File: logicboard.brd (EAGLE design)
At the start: 160 x 100 mm, 17 parts, among them U1 RASPBERRY_PI_CM-1-1376408-4, X3 PCI-60-POS-145167, X4 PCI-60-POS-145167, X5 PCI-60-POS-145167

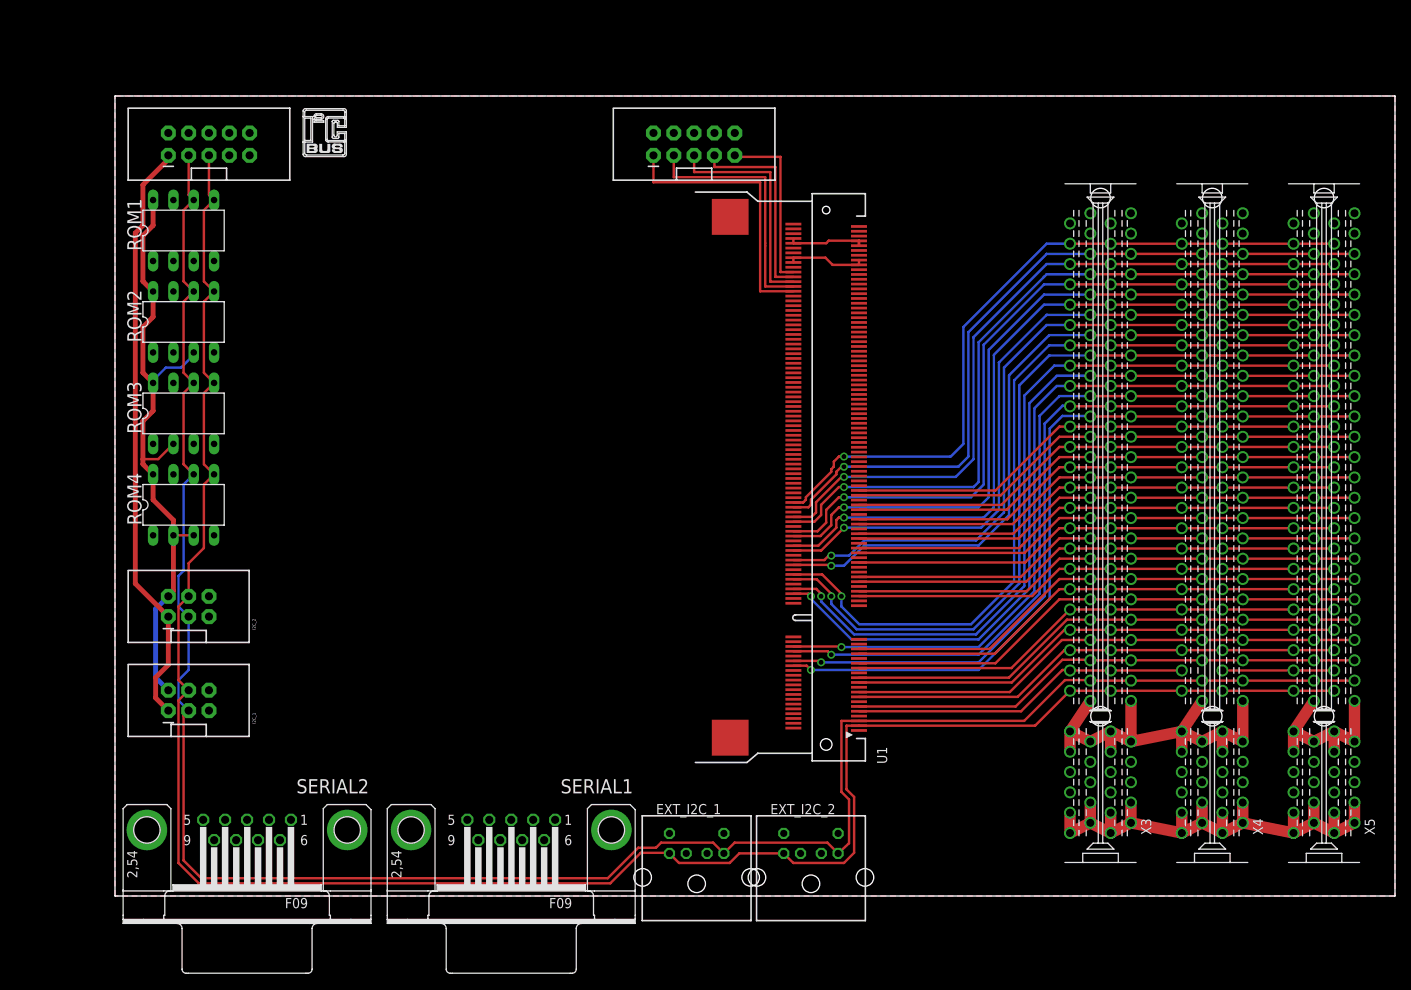
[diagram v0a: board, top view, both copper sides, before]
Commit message: Initial board, probably scrap
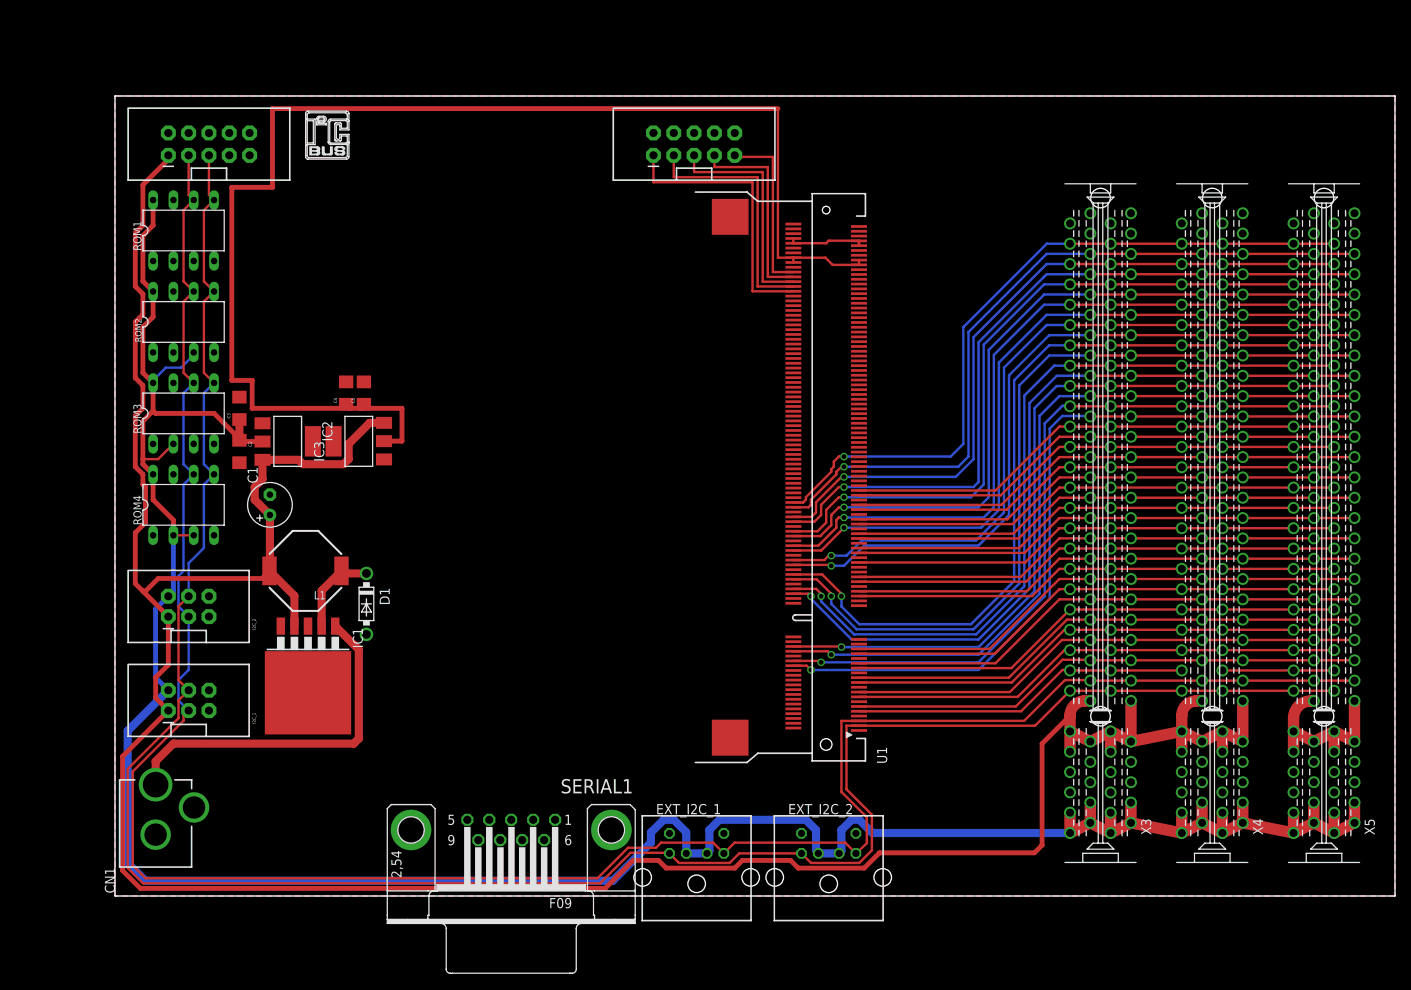
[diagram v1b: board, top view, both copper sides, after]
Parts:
- removed SERIAL2: (no value), con-subd:F09HP
- added C1: 220uf, rcl:E2,5-6
- added C2, C3, C4, C5: (no value), SparkFun-Capacitors:1206
- added CN1: (no value), adafruit:DCJACK_2MM_PTH
- added D1: 1N5824, diode:DO41-7.6
- added IC1: (no value), linear:TO263-5
- added IC2, IC3: REG1117, burr-brown:SOT223
- added L1: (no value), SparkFun-Passives:SRU1038
- moved EXT_I2C_2 2.22 mm to (89.2, -3.17)
- moved U$1 0.45 mm to (23.8, 92.1)
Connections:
- new net GNDBREAK: CN1.GNDBREAK
- new net V+: CN1.PWR, IC1.1
- new net VOUT: D1.C, IC1.2, L1.1
- net 1.8V: now also C4.1, C5.1, IC3.2
- net 3.3V: now also C2.1, C3.1, IC2.2
- net 5V: now also C1.+, IC1.4, IC2.3, IC3.3, L1.2
- net GND: now also C1.-, C2.2, C3.2, C4.2, C5.2, CN1.GND, D1.A, IC1.3, IC1.5, IC1.6, IC2.1, IC3.1
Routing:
- net 5V: track 150.4 -> 373.4 mm
- net 3.3V: track 160.4 -> 338.8 mm
- net 1.8V: track 9.77 -> 165.0 mm
- net V+: track 0.00 -> 44.8 mm
- net SCL: track 264.3 -> 276.8 mm
- net SDA: track 263.0 -> 275.3 mm
- net VOUT: track 0.00 -> 11.2 mm

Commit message: Initial commit
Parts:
- removed JP1: (no value), SparkFun-Connectors:2X5-SHROUDED_LOCK
- removed X3, X4, X5: PCI-60-POS-145167, con-amp:145167-2
- added AUDIO: (no value), SparkFun-Connectors:AUDIO-JACK
- added C10, C13: 0.01uf, SparkFun-Capacitors:CAP-PTH-SMALLEZ
- added C11, C14: 100uf, SparkFun-Capacitors:CAP-PTH-SMALLEZ
- added C12, C15: 0.001uf, SparkFun-Capacitors:CAP-PTH-SMALLEZ
- added C16, C17: (no value), SparkFun-Capacitors:1206
- added C6, C7: 10uf, SparkFun-Capacitors:CAP-PTH-SMALLEZ
- added C8, C9: 33n, SparkFun-Capacitors:CAP-PTH-SMALLEZ
- added CHEATER: (no value), SparkFun-Connectors:2X8
- added EXP1, EXP2, EXP3, EXP4, EXP5, EXP6, VIDEOCORE_JTAG: (no value), SparkFun-Connectors:2X5-SHROUDED_LOCK
- added H1, H2, H3, H4, H5, H6, H7, H8: MOUNT-HOLE4.5, holes:4,5
- added IC4: MCP2300X/P, adafruit:DIL18
- added IC5: REG1117, burr-brown:SOT223
- added PWR_SWITCH: (no value), SparkFun-Connectors:MOLEX-1X2
- added Q2: MOSFET-NCHANNELBS170, SparkFun-DiscreteSemi:TO-92
- added R1, R2: 10k, SparkFun-Resistors:AXIAL-0.3EZ
- added R3, R4: 150r, SparkFun-Resistors:AXIAL-0.3EZ
- added R5, R6: 270R, SparkFun-Resistors:AXIAL-0.3EZ
- added R7: (no value), SparkFun-Resistors:RPACK-SIP-PTH-8
- added R8, R9: (no value), SparkFun-Resistors:AXIAL-0.3EZ
- added SERIAL1_PORTFLIP, USB_POLARITY: FEMALE 2x3, SparkFun-Connectors:2X3
- added SPKR_L, SPKR_R: (no value), SparkFun-Connectors:JST-2-PTH-KIT
- added U$2: TDA7052, tda7052:DIL08
- U$1: value (none) -> TDA7052; device micro-philips:I2C -> tda7052:DIL08
- moved FRONTPANEL 131.6 mm to (137.8, 56.2), turned to 0 degrees
- moved L1 127.4 mm to (151.1, 37.5)
- moved IC1 127.3 mm to (151.4, 25.1)
- moved D1 126.7 mm to (158.1, 33.7)
- moved C1 123.7 mm to (142.6, 37.5), turned to 180 degrees
- moved C3 122.2 mm to (134.6, 33.7), turned to 0 degrees
- moved C2 121.5 mm to (134.6, 31.4), turned to 0 degrees
- moved U$1 120.4 mm to (144.1, 88.6), turned to 270 degrees
- moved IC2 116.2 mm to (133.3, 25.1), turned to 180 degrees
- moved C4 115.2 mm to (139.7, 31.4), turned to 180 degrees
- moved IC3 115.0 mm to (141.0, 25.1), turned to 180 degrees
- moved C5 112.4 mm to (139.7, 33.7), turned to 180 degrees
- moved EXT_I2C_2 94.7 mm to (-1.36, 24.4), turned to 270 degrees
- moved EXT_I2C_1 86.5 mm to (-1.36, 41.4), turned to 270 degrees
- moved SERIAL1 81.9 mm to (10.0, 80.0), turned to 90 degrees
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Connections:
- new net AUDIO_GROUND: C12.2, C15.2, Q2.1, U$1.3, U$1.6, U$2.3, U$2.6
- new net CPU_3.3V: C16.1, C17.1, IC5.2, U1.189, U1.190, U1.191, U1.192, U1.193, U1.194, U1.197, U1.198, U1.199, U1.200
- new net CTS: SERIAL1.8
- new net DCD: SERIAL1.1
- new net DSR: SERIAL1.6
- new net DTR: SERIAL1.4
- new net HDMI_CEC: CHEATER.15, U1.171
- new net HDMI_CK_N: CHEATER.2, U1.111
- new net HDMI_CK_P: CHEATER.4, U1.113
- new net HDMI_D0_N: CHEATER.6, U1.117
- new net HDMI_D0_P: CHEATER.8, U1.119
- new net HDMI_D1_N: CHEATER.10, U1.123
- new net HDMI_D1_P: CHEATER.12, U1.125
- new net HDMI_D2_N: CHEATER.14, U1.129
- new net HDMI_D2_P: CHEATER.16, U1.131
- new net HDMI_SCL: CHEATER.7, U1.175
- new net HDMI_SDA: CHEATER.11, U1.173
- new net IO_RST: IC4.6, R9.P$2
- new net LOUT_L: AUDIO.TIP, C12.1, C7.2, U$1.2
- new net LOUT_R: AUDIO.RING, C15.1, C6.2, U$2.2
- new net N$10: SPKR_L.2, U$1.5
- new net N$11: SPKR_L.1, U$1.8
- new net N$12: Q2.2, R8.P$2
- new net N$14: IC4.8
- new net N$16: IC4.15, R7.P$7
- new net N$17: IC4.14, R7.P$6
- new net N$18: IC4.13, R7.P$5
- new net N$19: IC4.12, R7.P$4
- new net N$20: IC4.11, R7.P$3
- new net N$21: IC4.10, R7.P$2
- new net N$22: SPKR_R.2, U$2.5
- new net N$23: SPKR_R.1, U$2.8
- new net N$7: U1.2
- new net N$8: CN1.PWR, PWR_SWITCH.1
- new net N$9: U1.168
- new net NC: EXP5.6
- new net PORT_RX: SERIAL1.2, SERIAL1_PORTFLIP.3
- new net PORT_TX: SERIAL1.3, SERIAL1_PORTFLIP.4
- new net PWM0_R: C6.1, C8.1, R3.P$2, R5.P$2
- new net PWM1_L: C7.1, C9.1, R4.P$2, R6.P$2
- new net RI: SERIAL1.9
- new net RTS: SERIAL1.7
- new net RUN: U1.177
- new net SPKR_ENABLE: IC4.17, R7.P$9, R8.P$1
- new net USB+: EXP5.10, USB_POLARITY.1, USB_POLARITY.6
- new net USB-: EXP5.9, USB_POLARITY.2, USB_POLARITY.5
- new net USB_D+: U1.165, USB_POLARITY.3
- new net USB_D-: U1.167, USB_POLARITY.4
- net 3.3V: now also EXP6.5, EXP6.6, IC4.18, R1.P$2, R2.P$2, R9.P$1; no longer EXT_I2C_1.1, EXT_I2C_1.2, EXT_I2C_2.1, EXT_I2C_2.2, U1.191, U1.192, U1.193, U1.194, X3.1, X3.2, X3.3, X3.4, X3.5, X3.6, X3.7, X3.8, X4.1, X4.2, X4.3, X4.4, X4.5, X4.6, X4.7, X4.8, X5.1, X5.2, X5.3, X5.4, X5.5, X5.6, X5.7, X5.8
- net 5V: now also C10.1, C11.1, C13.1, C14.1, EXP6.3, EXP6.4, EXT_I2C_1.1, EXT_I2C_1.2, EXT_I2C_2.1, EXT_I2C_2.2, IC5.3, U$1.1, U$2.1; no longer X3.17, X3.18, X3.19, X3.20, X3.21, X3.22, X3.23, X3.24, X4.17, X4.18, X4.19, X4.20, X4.21, X4.22, X4.23, X4.24, X5.17, X5.18, X5.19, X5.20, X5.21, X5.22, X5.23, X5.24
- net GND: now also AUDIO.SLEEVE, C10.2, C11.2, C13.2, C14.2, C16.2, C17.2, C8.2, C9.2, CHEATER.1, CHEATER.13, CHEATER.3, CHEATER.5, CHEATER.9, EXP5.7, EXP5.8, EXP6.1, EXP6.2, EXP6.7, EXP6.8, IC4.3, IC4.4, IC4.5, IC4.9, IC5.1, Q2.3, R3.P$1, R4.P$1, R7.P$1, SERIAL1.5, VIDEOCORE_JTAG.10, VIDEOCORE_JTAG.2, VIDEOCORE_JTAG.4, VIDEOCORE_JTAG.6, VIDEOCORE_JTAG.8; no longer JP1.10, JP1.2, JP1.4, JP1.6, JP1.8, X3.10, X3.11, X3.12, X3.13, X3.14, X3.15, X3.16, X3.9, X4.10, X4.11, X4.12, X4.13, X4.14, X4.15, X4.16, X4.9, X5.10, X5.11, X5.12, X5.13, X5.14, X5.15, X5.16, X5.9
- net GPIO10: now also EXP2.1; no longer X3.45, X3.46, X4.45, X4.46, X5.45, X5.46
- net GPIO11: now also EXP2.2; no longer X3.47, X3.48, X4.47, X4.48, X5.47, X5.48
- net GPIO12: now also EXP2.3; no longer X3.49, X3.50, X4.49, X4.50, X5.49, X5.50
- net GPIO13: now also EXP2.4; no longer X3.51, X3.52, X4.51, X4.52, X5.51, X5.52
- net GPIO17: now also EXP2.7; no longer X3.57, X3.58, X4.57, X4.58, X5.57, X5.58
- net GPIO18: now also EXP2.8; no longer X3.59, X3.60, X4.59, X4.60, X5.59, X5.60
- net GPIO19: now also EXP2.9; no longer X3.61, X3.62, X4.61, X4.62, X5.61, X5.62
- net GPIO20: now also EXP2.10; no longer X3.63, X3.64, X4.63, X4.64, X5.63, X5.64
- net GPIO21: now also EXP3.1; no longer X3.65, X3.66, X4.65, X4.66, X5.65, X5.66
- net GPIO22: now also EXP3.2; no longer X3.67, X3.68, X4.67, X4.68, X5.67, X5.68
- net GPIO23: now also EXP3.3; no longer X3.69, X3.70, X4.69, X4.70, X5.69, X5.70
- net GPIO24: now also EXP3.4; no longer X3.71, X3.72, X4.71, X4.72, X5.71, X5.72
- net GPIO25: now also EXP3.5; no longer X3.73, X3.74, X4.73, X4.74, X5.73, X5.74
- net GPIO26: now also EXP3.6; no longer X3.75, X3.76, X4.75, X4.76, X5.75, X5.76
- net GPIO27: now also EXP3.7; no longer X3.77, X3.78, X4.77, X4.78, X5.77, X5.78
- net GPIO28: now also EXP3.8; no longer X3.79, X3.80, X4.79, X4.80, X5.79, X5.80
- net GPIO29: now also EXP3.9; no longer X3.81, X3.82, X4.81, X4.82, X5.81, X5.82
- net GPIO30: now also EXP3.10; no longer X3.83, X3.84, X4.83, X4.84, X5.83, X5.84
- net GPIO31: now also EXP4.1; no longer X3.85, X3.86, X4.85, X4.86, X5.85, X5.86
- net GPIO32: now also EXP4.2; no longer X3.87, X3.88, X4.87, X4.88, X5.87, X5.88
- net GPIO33: now also EXP4.3; no longer X3.89, X3.90, X4.89, X4.90, X5.89, X5.90
- net GPIO34: now also EXP4.4; no longer X3.91, X3.92, X4.91, X4.92, X5.91, X5.92
- net GPIO35: now also EXP4.5; no longer X3.93, X3.94, X4.93, X4.94, X5.93, X5.94
- net GPIO36: now also EXP4.6; no longer X3.95, X3.96, X4.95, X4.96, X5.95, X5.96
- net GPIO37: now also EXP4.7; no longer X3.97, X3.98, X4.97, X4.98, X5.97, X5.98
- net GPIO38: now also EXP4.8; no longer X3.100, X3.99, X4.100, X4.99, X5.100, X5.99
- net GPIO39: now also EXP4.9; no longer X3.101, X3.102, X4.101, X4.102, X5.101, X5.102
- net GPIO4: now also EXP1.5; no longer X3.33, X3.34, X4.33, X4.34, X5.33, X5.34
- net GPIO40: now also EXP4.10, R5.P$1; no longer X3.103, X3.104, X4.103, X4.104, X5.103, X5.104
- net GPIO41: now also EXP5.1, R6.P$1; no longer X3.105, X3.106, X4.105, X4.106, X5.105, X5.106
- net GPIO42: now also EXP5.2; no longer X3.107, X3.108, X4.107, X4.108, X5.107, X5.108
- net GPIO43: now also EXP5.3; no longer X3.109, X3.110, X4.109, X4.110, X5.109, X5.110
- net GPIO44: now also EXP5.4; no longer X3.111, X3.112, X4.111, X4.112, X5.111, X5.112
- net GPIO45: now also EXP5.5; no longer X3.113, X3.114, X4.113, X4.114, X5.113, X5.114
- net GPIO5: now also EXP1.6; no longer X3.35, X3.36, X4.35, X4.36, X5.35, X5.36
- net GPIO6: now also EXP1.7; no longer X3.37, X3.38, X4.37, X4.38, X5.37, X5.38
- net GPIO7: now also EXP1.8; no longer X3.39, X3.40, X4.39, X4.40, X5.39, X5.40
- net GPIO8: now also EXP1.9; no longer X3.41, X3.42, X4.41, X4.42, X5.41, X5.42
- net GPIO9: now also EXP1.10; no longer X3.43, X3.44, X4.43, X4.44, X5.43, X5.44
- net LED_NOTIFICATION: now also IC4.16, R7.P$8
- net N$1: now also VIDEOCORE_JTAG.9; no longer JP1.9
- net N$2: now also VIDEOCORE_JTAG.7; no longer JP1.7
- net N$3: now also VIDEOCORE_JTAG.5; no longer JP1.5
- net N$4: now also VIDEOCORE_JTAG.3; no longer JP1.3
- net N$5: now also VIDEOCORE_JTAG.1; no longer JP1.1
- net RXD0: now also EXP2.6, SERIAL1_PORTFLIP.1, SERIAL1_PORTFLIP.6; no longer X3.55, X3.56, X4.55, X4.56, X5.55, X5.56
- net SCL: now also EXP1.2, IC4.1, R1.P$1; no longer X3.27, X3.28, X4.27, X4.28, X5.27, X5.28
- net SCL1: now also EXP1.4; no longer X3.31, X3.32, X4.31, X4.32, X5.31, X5.32
- net SDA: now also EXP1.1, IC4.2, R2.P$1; no longer X3.25, X3.26, X4.25, X4.26, X5.25, X5.26
- net SDA1: now also EXP1.3; no longer X3.29, X3.30, X4.29, X4.30, X5.29, X5.30
- net TXD0: now also EXP2.5, SERIAL1_PORTFLIP.2, SERIAL1_PORTFLIP.5; no longer X3.53, X3.54, X4.53, X4.54, X5.53, X5.54
- net V+: now also EXP6.10, EXP6.9, PWR_SWITCH.2; no longer CN1.PWR
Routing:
- net LOUT_R: track 0.00 -> 173.7 mm
- net LOUT_L: track 0.00 -> 170.5 mm, vias 0 -> 1
- net N$8: track 0.00 -> 155.6 mm
- net 1.8V: track 165.0 -> 64.3 mm
- net SDA: track 275.3 -> 369.9 mm, vias 0 -> 3
- net SCL: track 276.8 -> 357.7 mm
- net TXD0: track 61.1 -> 132.0 mm
- net RXD0: track 63.9 -> 127.7 mm
- net 3.3V: track 338.8 -> 282.7 mm, vias 0 -> 3
- net USB-: track 0.00 -> 55.4 mm
- net USB+: track 0.00 -> 55.0 mm
- net SPKR_ENABLE: track 0.00 -> 55.0 mm, vias 0 -> 1
- net GPIO34: track 102.2 -> 49.8 mm
- net LED_NOTIFICATION: track 0.00 -> 52.1 mm
- net GPIO32: track 99.9 -> 51.2 mm
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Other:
- board size 160 x 100 mm -> 160 x 110 mm
- board text added: "EXP1"
- board text added: "EXP2"
- board text added: "EXP3"
- board text added: "EXP4"
- board text added: "EXP5"
- board text added: "EXP6"
- board text added: "FRONT PANEL"
- board text added: "I2C A"
- board text added: "I2C B"
- board text added: "I2C EXPANSION CARD"
- board text added: "POWER SWITCH"
- board text added: "REAR"
- board text added: "VIDEO CORE JTAG"

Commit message: for now, a complete logic board and expansion board until I find something wrong with it
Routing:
- net 3.3V: track 282.7 -> 292.8 mm
- net CPU_3.3V: track 46.3 -> 46.9 mm
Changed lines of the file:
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@@
 <grid distance="0.0125" unitdist="inch" unit="mm" style="lines" multiple="1" display="no" altdistance="0.025" altunitdist="inch" altunit="inch"/>
 <layers>
-<layer number="1" name="Top" color="4" fill="1" visible="no" active="yes"/>
+<layer number="1" name="Top" color="4" fill="1" visible="yes" active="yes"/>
 <layer number="2" name="Route2" color="1" fill="3" visible="no" active="no"/>
 <layer number="3" name="Route3" color="4" fill="3" visible="no" active="no"/>
@@
 <wire x1="133.3246" y1="31.3279" x2="133.22" y2="31.4325" width="1.016" layer="1"/>
 <wire x1="125" y1="16.397" x2="125" y2="25.305" width="1.016" layer="1"/>
-<wire x1="125" y1="25.305" x2="129.8575" y2="30.1625" width="1.016" layer="1"/>
+<wire x1="125" y1="25.305" x2="126.6825" y2="26.9875" width="1.016" layer="1"/>
+<wire x1="126.6825" y1="26.9875" x2="129.8575" y2="30.1625" width="1.016" layer="1"/>
 <wire x1="129.8575" y1="30.1625" x2="133.3246" y2="30.1625" width="1.016" layer="1"/>
 <wire x1="125" y1="16.397" x2="125" y2="13.603" width="1.016" layer="1"/>
@@
 <wire x1="133.6675" y1="40.3225" x2="130.175" y2="43.815" width="0.4064" layer="1"/>
 <wire x1="130.175" y1="43.815" x2="130.175" y2="45.4025" width="0.4064" layer="1"/>
-<wire x1="130.175" y1="45.4025" x2="129.8575" y2="45.4025" width="0.4064" layer="1"/>
-<wire x1="129.8575" y1="45.4025" x2="128.5875" y2="45.4025" width="0.4064" layer="1"/>
+<wire x1="130.175" y1="45.4025" x2="128.5875" y2="45.4025" width="0.4064" layer="1"/>
 <wire x1="128.5875" y1="45.4025" x2="124.46" y2="49.53" width="0.4064" layer="1"/>
 <wire x1="46.0375" y1="42.545" x2="49.2125" y2="45.72" width="0.4064" layer="16"/>
@@
 <wire x1="110.8075" y1="29.21" x2="114.3" y2="29.21" width="0.254" layer="1"/>
 <wire x1="114.3" y1="29.21" x2="116.205" y2="31.115" width="0.254" layer="1"/>
-<wire x1="116.205" y1="31.115" x2="116.205" y2="41.5925" width="0.254" layer="1"/>
-<wire x1="116.205" y1="41.5925" x2="117.7925" y2="43.18" width="0.254" layer="1"/>
 <wire x1="117.7925" y1="43.18" x2="120.015" y2="43.18" width="0.254" layer="1"/>
-<wire x1="117.7925" y1="43.18" x2="117.7925" y2="45.3" width="0.254" layer="1"/>
 <wire x1="124.46" y1="49.53" x2="115.57" y2="49.53" width="0.4064" layer="1"/>
 <wire x1="115.57" y1="49.53" x2="114.3" y2="50.8" width="0.4064" layer="1"/>
-<wire x1="115.57" y1="49.53" x2="117.7925" y2="45.3" width="0" layer="19" extent="1-1"/>
+<wire x1="117.7925" y1="43.18" x2="116.205" y2="41.5925" width="0.254" layer="1"/>
+<wire x1="116.205" y1="41.5925" x2="116.205" y2="31.115" width="0.254" layer="1"/>
+<wire x1="116.205" y1="31.115" x2="118.11" y2="29.21" width="0.254" layer="1"/>
+<wire x1="118.11" y1="29.21" x2="124.1425" y2="29.21" width="0.254" layer="1"/>
+<wire x1="124.1425" y1="29.21" x2="126.365" y2="26.9875" width="0.254" layer="1"/>
+<wire x1="126.365" y1="26.9875" x2="126.6825" y2="26.9875" width="0.254" layer="1"/>
 </signal>
 <signal name="5V">
@@
 <wire x1="128.5621" y1="44.2879" x2="128.7175" y2="44.1325" width="0.4064" layer="1"/>
 <wire x1="128.7175" y1="44.1325" x2="128.7175" y2="41.91" width="0.4064" layer="1"/>
-<wire x1="113.675" y1="47.0175" x2="114.275" y2="47.0175" width="0" layer="19" extent="1-1"/>
+<wire x1="113.675" y1="47.0175" x2="114.275" y2="47.0175" width="0.4064" layer="1"/>
 </signal>
 </signals>
